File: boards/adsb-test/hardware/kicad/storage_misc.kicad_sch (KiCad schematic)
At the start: 0 parts

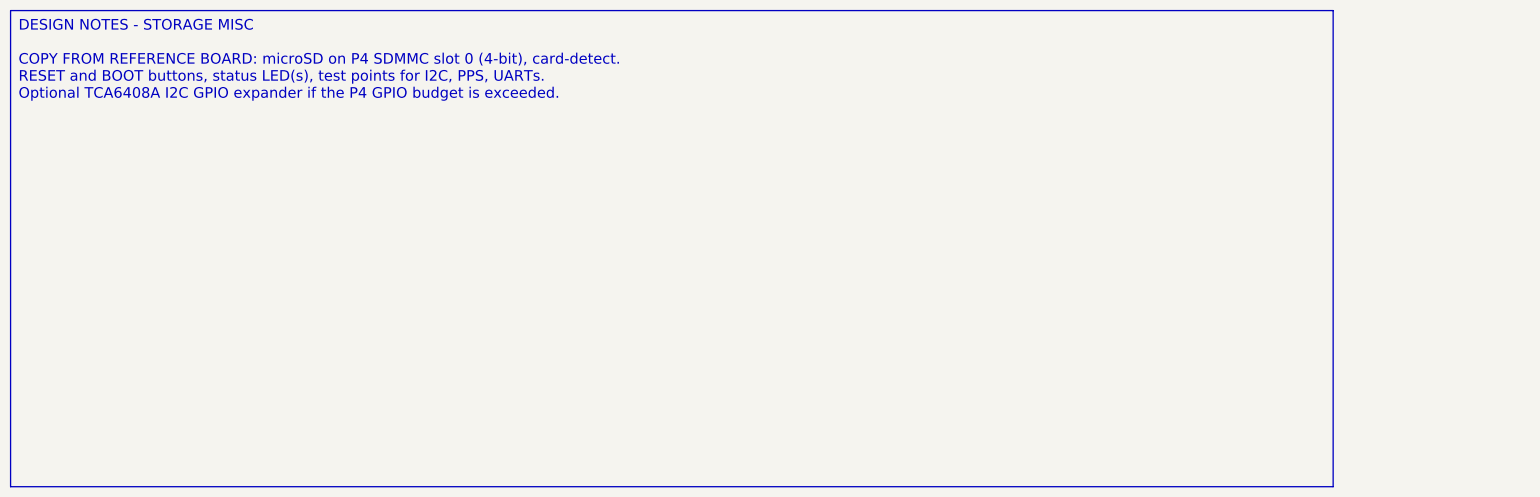
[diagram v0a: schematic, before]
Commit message: Release v0.4.0: ADSB_Test with ESP32-C5, ADSBee m1421 and LA5016 header
- C6 -> C5 co-processor; m1421 identified and integrated (symbol/footprint
  from the ADSBee 1421 carrier, GPL-3.0 attribution)
- Power budget and 2S1P battery sizing for >= 1 h; USB-A for 1-2 SDRs via hub
- Dev port: FT2232H + RP2040 debugprobe; TCA6408A expander for slow I/O
- Test Debug sheet with LA5016 header and rail test points
- Vendor documents git-ignored (public repo)

Co-Authored-By: Claude Opus 5.5 <noreply@anthropic.com>
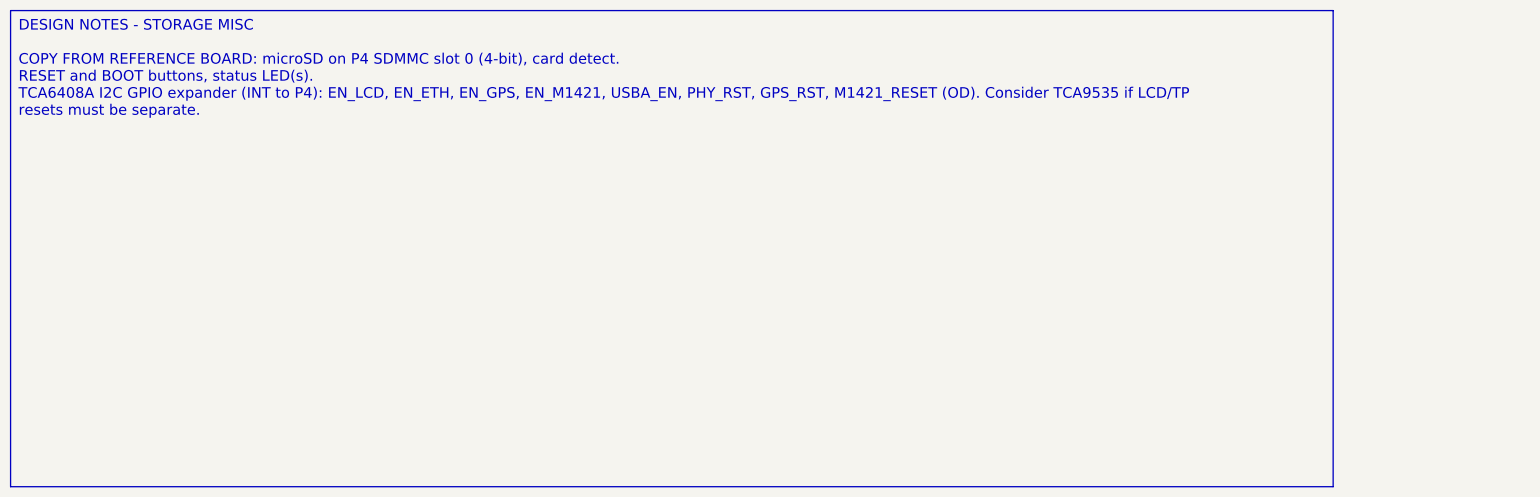
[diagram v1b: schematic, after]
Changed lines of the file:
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@@
 		(comment 1 "Requirements: boards/adsb-test/docs/requirements.md")
 	)
-	(text_box "DESIGN NOTES - STORAGE MISC\n\nCOPY FROM REFERENCE BOARD: microSD on P4 SDMMC slot 0 (4-bit), card-detect.\nRESET and BOOT buttons, status LED(s), test points for I2C, PPS, UARTs.\nOptional TCA6408A I2C GPIO expander if the P4 GPIO budget is exceeded."
+	(text_box "DESIGN NOTES - STORAGE MISC\n\nCOPY FROM REFERENCE BOARD: microSD on P4 SDMMC slot 0 (4-bit), card detect.\nRESET and BOOT buttons, status LED(s).\nTCA6408A I2C GPIO expander (INT to P4): EN_LCD, EN_ETH, EN_GPS, EN_M1421, USBA_EN, PHY_RST, GPS_RST, M1421_RESET (OD). Consider TCA9535 if LCD/TP resets must be separate."
 		(exclude_from_sim no)
 		(at 20 20 0)
